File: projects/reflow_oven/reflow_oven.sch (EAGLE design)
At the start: 5 parts, among them IC1 MEGA32-A, IC3 FT232RL, X1 MINI-USB_SHIELD5P4-32005-400

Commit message: think the ftdi chip is done.  also did a good deal of the arduino setup.
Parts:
- added C2, C4, C9: 0.1uF, rcl:C-EUC0805
- added C3, C7, C8: 10uF, adafruit:CPOL-US175TMP-0810
- added C5, C6: 22pF, rcl:C-EUC0805
- added IC2: 7805DT, linear:7805DT
- added LED1: Red, led:LEDCHIPLED_0603
- added LED2: Green, led:LEDCHIPLED_0603
- added POWERLED: Green, adafruit:LEDCHIP-LED0805
- added R1, R2: 1k, resistor:R-US_R0805
- added R3: 10k, resistor:R-US_R0805
- added R4: 150, resistor:R-US_R0805
- added X2: 16.000MHz, adafruit:XTALNX8045
- C1: value (none) -> 0.1uF; device rcl:C-USC0805K -> rcl:C-EUC0805
- X1: value MINI-USB_SHIELD5P4-32005-400 -> USB; device con-cypressindustries:MINI-USB_SHIELD5P4-32005-400 -> con-cypressindustries:MINI-USB-32005-201
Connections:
- net RXD renamed 0
- net TXD renamed 1
- new net 10: IC1.(AIN0/INT2)PB2
- new net 11: IC1.(AIN1/OC0)PB3
- new net 12: IC1.(SS)PB4
- new net 13: IC1.(MOSI)PB5
- new net 8: IC1.(T0/XCK)PB0
- new net 9: IC1.(T1)PB1
- new net A1: IC1.(TDO)PC4
- new net A2: IC1.(TMS)PC3
- new net A3: IC1.(TCK)PC2
- new net A4: IC1.PC1(SDA)
- new net A5: IC1.PC0(SCL)
- new net D+DP: IC3.USBDP, X1.3
- new net D-DM: IC3.USBDM, X1.2
- new net DTR: C4.2, IC3.!DTR
- new net N$1: C5.2, IC1.XTAL2, X2.P$2
- new net N$10: IC1.(ICP)PD6
- new net N$11: IC1.(OC2)PD7
- new net N$17: IC1.(TDI)PC5
- new net N$18: IC1.(TOSC1)PC6
- new net N$19: IC1.(TOSC2)PC7
- new net N$2: C6.2, IC1.XTAL1, X2.P$1
- new net N$4: LED1.A, R1.1
- new net N$5: POWERLED.C, R4.2
- new net N$6: IC1.(INT0)PD2
- new net N$7: IC1.(INT1)PD3
- new net N$8: IC1.(OC1B)PD4
- new net N$9: IC1.(OC1A)PD5
- new net POWER: IC3.VCCIO
- new net RXLED: IC3.CBUS1, LED2.C
- new net TXLED: IC3.CBUS0, LED1.C
- new net VCCIO: C1.1, IC3.3V3OUT
- new net VIN: C7.+, IC2.VI
- new net VOUT: C8.+, IC2.VO, POWERLED.A
- net GND: now also C1.2, C2.2, C3.-, C5.1, C6.1, C7.-, C8.-, C9.1, IC2.GND, IC3.TEST, R4.1, X1.5
- net N$3: now also LED2.A, R2.1; no longer C1.1, IC3.!RESET
- net RESET: now also C4.1, R3.2; no longer C1.2
- net VCC: now also C2.1, C3.+, C9.2, IC1.AREF, IC3.VCC, R1.2, R2.2, R3.1, X1.1
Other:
- note added: "3.3V"
- note added: "Check These Names"

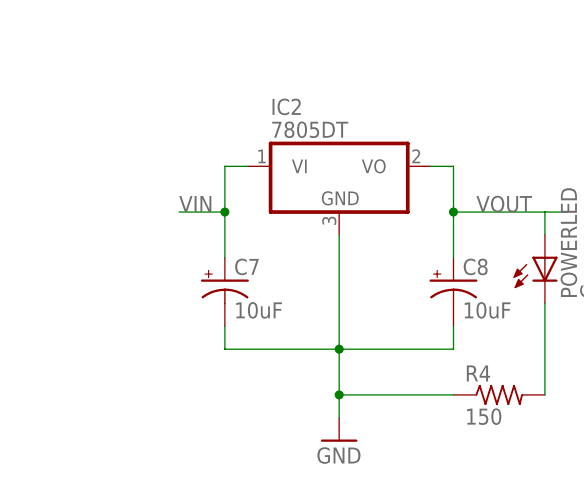
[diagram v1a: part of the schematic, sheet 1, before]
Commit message: add DC Jack
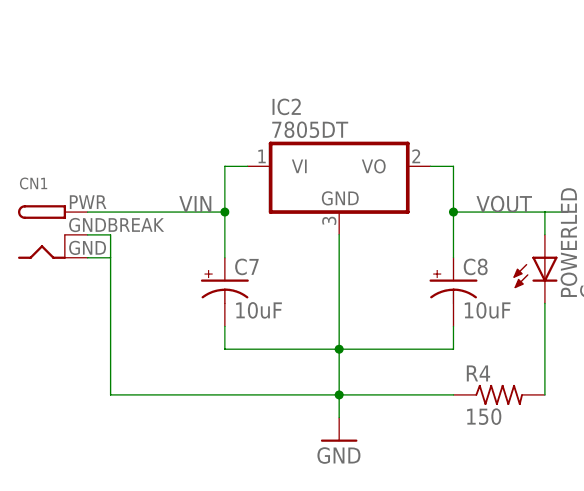
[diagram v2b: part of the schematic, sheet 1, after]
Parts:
- added CN1: (no value), adafruit:DCBARRELPTH
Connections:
- net GND: now also CN1.GND, CN1.GNDBREAK
- net VIN: now also CN1.PWR
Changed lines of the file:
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@@
 <grid distance="0.1" unitdist="inch" unit="inch" style="lines" multiple="1" display="no" altdistance="0.01" altunitdist="inch" altunit="inch"/>
 <layers>
-<layer number="1" name="Top" color="4" fill="1" visible="yes" active="no"/>
-<layer number="2" name="Route2" color="1" fill="3" visible="yes" active="no"/>
-<layer number="3" name="Route3" color="4" fill="3" visible="yes" active="no"/>
-<layer number="4" name="Route4" color="1" fill="4" visible="yes" active="no"/>
-<layer number="5" name="Route5" color="4" fill="4" visible="yes" active="no"/>
-<layer number="6" name="Route6" color="1" fill="8" visible="yes" active="no"/>
-<layer number="7" name="Route7" color="4" fill="8" visible="yes" active="no"/>
-<layer number="8" name="Route8" color="1" fill="2" visible="yes" active="no"/>
-<layer number="9" name="Route9" color="4" fill="2" visible="yes" active="no"/>
-<layer number="10" name="Route10" color="1" fill="7" visible="yes" active="no"/>
-<layer number="11" name="Route11" color="4" fill="7" visible="yes" active="no"/>
-<layer number="12" name="Route12" color="1" fill="5" visible="yes" active="no"/>
-<layer number="13" name="Route13" color="4" fill="5" visible="yes" active="no"/>
-<layer number="14" name="Route14" color="1" fill="6" visible="yes" active="no"/>
-<layer number="15" name="Route15" color="4" fill="6" visible="yes" active="no"/>
-<layer number="16" name="Bottom" color="1" fill="1" visible="yes" active="no"/>
-<layer number="17" name="Pads" color="2" fill="1" visible="yes" active="no"/>
-<layer number="18" name="Vias" color="2" fill="1" visible="yes" active="no"/>
-<layer number="19" name="Unrouted" color="6" fill="1" visible="yes" active="no"/>
-<layer number="20" name="Dimension" color="15" fill="1" visible="yes" active="no"/>
-<layer number="21" name="tPlace" color="7" fill="1" visible="yes" active="no"/>
-<layer number="22" name="bPlace" color="7" fill="1" visible="yes" active="no"/>
-<layer number="23" name="tOrigins" color="15" fill="1" visible="yes" active="no"/>
-<layer number="24" name="bOrigins" color="15" fill="1" visible="yes" active="no"/>
-<layer number="25" name="tNames" color="7" fill="1" visible="yes" active="no"/>
-<layer number="26" name="bNames" color="7" fill="1" visible="yes" active="no"/>
-<layer number="27" name="tValues" color="7" fill="1" visible="yes" active="no"/>
-<layer number="28" name="bValues" color="7" fill="1" visible="yes" active="no"/>
+<layer number="1" name="Top" color="4" fill="1" visible="no" active="no"/>
+<layer number="2" name="Route2" color="1" fill="3" visible="no" active="no"/>
+<layer number="3" name="Route3" color="4" fill="3" visible="no" active="no"/>
+<layer number="4" name="Route4" color="1" fill="4" visible="no" active="no"/>
+<layer number="5" name="Route5" color="4" fill="4" visible="no" active="no"/>
+<layer number="6" name="Route6" color="1" fill="8" visible="no" active="no"/>
+<layer number="7" name="Route7" color="4" fill="8" visible="no" active="no"/>
+<layer number="8" name="Route8" color="1" fill="2" visible="no" active="no"/>
+<layer number="9" name="Route9" color="4" fill="2" visible="no" active="no"/>
+<layer number="10" name="Route10" color="1" fill="7" visible="no" active="no"/>
+<layer number="11" name="Route11" color="4" fill="7" visible="no" active="no"/>
+<layer number="12" name="Route12" color="1" fill="5" visible="no" active="no"/>
+<layer number="13" name="Route13" color="4" fill="5" visible="no" active="no"/>
+<layer number="14" name="Route14" color="1" fill="6" visible="no" active="no"/>
+<layer number="15" name="Route15" color="4" fill="6" visible="no" active="no"/>
+<layer number="16" name="Bottom" color="1" fill="1" visible="no" active="no"/>
+<layer number="17" name="Pads" color="2" fill="1" visible="no" active="no"/>
+<layer number="18" name="Vias" color="2" fill="1" visible="no" active="no"/>
+<layer number="19" name="Unrouted" color="6" fill="1" visible="no" active="no"/>
+<layer number="20" name="Dimension" color="15" fill="1" visible="no" active="no"/>
+<layer number="21" name="tPlace" color="7" fill="1" visible="no" active="no"/>
+<layer number="22" name="bPlace" color="7" fill="1" visible="no" active="no"/>
+<layer number="23" name="tOrigins" color="15" fill="1" visible="no" active="no"/>
+<layer number="24" name="bOrigins" color="15" fill="1" visible="no" active="no"/>
+<layer number="25" name="tNames" color="7" fill="1" visible="no" active="no"/>
+<layer number="26" name="bNames" color="7" fill="1" visible="no" active="no"/>
+<layer number="27" name="tValues" color="7" fill="1" visible="no" active="no"/>
+<layer number="28" name="bValues" color="7" fill="1" visible="no" active="no"/>
 <layer number="29" name="tStop" color="7" fill="3" visible="no" active="no"/>
 <layer number="30" name="bStop" color="7" fill="6" visible="no" active="no"/>
@@
 <layer number="35" name="tGlue" color="7" fill="4" visible="no" active="no"/>
 <layer number="36" name="bGlue" color="7" fill="5" visible="no" active="no"/>
-<layer number="37" name="tTest" color="7" fill="1" visible="yes" active="no"/>
-<layer number="38" name="bTest" color="7" fill="1" visible="yes" active="no"/>
+<layer number="37" name="tTest" color="7" fill="1" visible="no" active="no"/>
+<layer number="38" name="bTest" color="7" fill="1" visible="no" active="no"/>
 <layer number="39" name="tKeepout" color="4" fill="11" visible="no" active="no"/>
 <layer number="40" name="bKeepout" color="1" fill="11" visible="no" active="no"/>
@@
 <layer number="44" name="Drills" color="7" fill="1" visible="no" active="no"/>
 <layer number="45" name="Holes" color="7" fill="1" visible="no" active="no"/>
-<layer number="46" name="Milling" color="3" fill="1" visible="yes" active="no"/>
-<layer number="47" name="Measures" color="7" fill="1" visible="yes" active="no"/>
-<layer number="48" name="Document" color="7" fill="1" visible="yes" active="no"/>
-<layer number="49" name="Reference" color="7" fill="1" visible="yes" active="no"/>
-<layer number="50" name="dxf" color="7" fill="1" visible="yes" active="no"/>
-<layer number="51" name="tDocu" color="7" fill="1" visible="yes" active="no"/>
-<layer number="52" name="bDocu" color="7" fill="1" visible="yes" active="no"/>
-<layer number="53" name="tGND_GNDA" color="7" fill="9" visible="yes" active="no"/>
-<layer number="54" name="bGND_GNDA" color="1" fill="9" visible="yes" active="no"/>
-<layer number="56" name="wert" color="7" fill="1" visible="yes" active="no"/>
+<layer number="46" name="Milling" color="3" fill="1" visible="no" active="no"/>
+<layer number="47" name="Measures" color="7" fill="1" visible="no" active="no"/>
+<layer number="48" name="Document" color="7" fill="1" visible="no" active="no"/>
+<layer number="49" name="Reference" color="7" fill="1" visible="no" active="no"/>
+<layer number="50" name="dxf" color="7" fill="1" visible="no" active="no"/>
+<layer number="51" name="tDocu" color="7" fill="1" visible="no" active="no"/>
+<layer number="52" name="bDocu" color="7" fill="1" visible="no" active="no"/>
+<layer number="53" name="tGND_GNDA" color="7" fill="9" visible="no" active="no"/>
+<layer number="54" name="bGND_GNDA" color="1" fill="9" visible="no" active="no"/>
+<layer number="56" name="wert" color="7" fill="1" visible="no" active="no"/>
 <layer number="91" name="Nets" color="2" fill="1" visible="yes" active="yes"/>
 <layer number="92" name="Busses" color="1" fill="1" visible="yes" active="yes"/>
@@
 <part name="C9" library="rcl" deviceset="C-EU" device="C0805" value="0.1uF"/>
 <part name="GND4" library="supply1" deviceset="GND" device=""/>
+<part name="CN1" library="adafruit" deviceset="DCBARREL" device="PTH"/>
 </parts>
 <sheets>
@@
 </instance>
 <instance part="GND4" gate="1" x="88.9" y="111.76"/>
+<instance part="CN1" gate="G$1" x="20.32" y="76.2"/>
 </instances>
 <busses>
@@
 <wire x1="63.5" y1="58.42" x2="50.8" y2="58.42" width="0.1524" layer="91"/>
 <junction x="50.8" y="58.42"/>
+<pinref part="CN1" gate="G$1" pin="GNDBREAK"/>
+<wire x1="22.86" y1="76.2" x2="25.4" y2="76.2" width="0.1524" layer="91"/>
+<wire x1="25.4" y1="76.2" x2="25.4" y2="73.66" width="0.1524" layer="91"/>
+<pinref part="CN1" gate="G$1" pin="GND"/>
+<wire x1="25.4" y1="73.66" x2="22.86" y2="73.66" width="0.1524" layer="91"/>
+<wire x1="25.4" y1="73.66" x2="25.4" y2="58.42" width="0.1524" layer="91"/>
+<wire x1="25.4" y1="58.42" x2="50.8" y2="58.42" width="0.1524" layer="91"/>
 </segment>
 <segment>
@@
 <junction x="38.1" y="78.74"/>
 <wire x1="38.1" y1="78.74" x2="38.1" y2="73.66" width="0.1524" layer="91"/>
-<wire x1="38.1" y1="78.74" x2="33.02" y2="78.74" width="0.1524" layer="91"/>
 <label x="33.02" y="78.74" size="1.778" layer="95"/>
-</segment>
-</net>
+<pinref part="CN1" gate="G$1" pin="PWR"/>
+<wire x1="22.86" y1="78.74" x2="38.1" y2="78.74" width="0.1524" layer="91"/>
+</segment>
+</net>

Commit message: button debounce start
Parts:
- added C10, C11: 1uF, resistor:C-USC0805
- added C12: 100nF, resistor:C-USC0805
- added D1, D2: (no value), adafruit:DIODESMA
- added IC4: 74HC14D, 74xx-eu:74HC14D
- added R5, R6: 82k, resistor:R-US_R0805
- added R7, R8: 18k, resistor:R-US_R0805
- added S2, S3: (no value), switch-omron:10-XX
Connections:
- new net 2: IC4B.O
- new net 3: IC4A.O
- new net N$12: D1.A, R5.2, R8.1, S2.S, S2.S1
- new net N$13: C11.1, D1.C, IC4A.I, R8.2
- new net N$14: D2.A, R6.2, R7.1, S3.S, S3.S1
- new net N$15: C10.1, D2.C, IC4B.I, R7.2
- net GND: now also C10.2, C11.2, C12.2, IC4P.GND, S2.P, S2.P1, S3.P, S3.P1
- net VCC: now also C12.1, IC4P.VCC, R5.1, R6.1
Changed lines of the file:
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@@
 <part name="GND4" library="supply1" deviceset="GND" device=""/>
 <part name="CN1" library="adafruit" deviceset="DCBARREL" device="PTH"/>
+<part name="IC4" library="74xx-eu" deviceset="74*14" device="D" technology="HC"/>
+<part name="P+5" library="supply1" deviceset="VCC" device=""/>
+<part name="P+9" library="supply1" deviceset="VCC" device=""/>
+<part name="R5" library="resistor" deviceset="R-US_" device="R0805" value="82k"/>
+<part name="R8" library="resistor" deviceset="R-US_" device="R0805" value="18k"/>
+<part name="GND13" library="supply1" deviceset="GND" device=""/>
+<part name="GND14" library="supply1" deviceset="GND" device=""/>
+<part name="D1" library="adafruit" deviceset="DIODE" device="SMA"/>
+<part name="C11" library="resistor" deviceset="C-US" device="C0805" value="1uF"/>
+<part name="C12" library="resistor" deviceset="C-US" device="C0805" value="100nF"/>
+<part name="S2" library="switch-omron" deviceset="10-XX" device=""/>
+<part name="P+10" library="supply1" deviceset="VCC" device=""/>
+<part name="R6" library="resistor" deviceset="R-US_" device="R0805" value="82k"/>
+<part name="R7" library="resistor" deviceset="R-US_" device="R0805" value="18k"/>
+<part name="GND15" library="supply1" deviceset="GND" device=""/>
+<part name="D2" library="adafruit" deviceset="DIODE" device="SMA"/>
+<part name="C10" library="resistor" deviceset="C-US" device="C0805" value="1uF"/>
+<part name="S3" library="switch-omron" deviceset="10-XX" device=""/>
+<part name="FRAME4" library="frames" deviceset="DINA4_L" device=""/>
+<part name="FRAME5" library="frames" deviceset="LETTER_P" device=""/>
 </parts>
 <sheets>
@@
 </nets>
 </sheet>
+<sheet>
+<description>button debounce</description>
+<plain>
+</plain>
+<instances>
+<instance part="IC4" gate="A" x="99.06" y="132.08"/>
+<instance part="IC4" gate="B" x="99.06" y="96.52"/>
+<instance part="P+5" gate="VCC" x="25.4" y="157.48"/>
+<instance part="P+9" gate="VCC" x="147.32" y="149.86"/>
+<instance part="R5" gate="G$1" x="35.56" y="147.32"/>
+<instance part="R8" gate="G$1" x="50.8" y="137.16"/>
+<instance part="GND13" gate="1" x="147.32" y="119.38"/>
+<instance part="GND14" gate="1" x="50.8" y="116.84"/>
+<instance part="D1" gate="G$1" x="50.8" y="147.32"/>
+<instance part="C11" gate="G$1" x="58.42" y="132.08"/>
+<instance part="C12" gate="G$1" x="152.4" y="137.16"/>
+<instance part="S2" gate="1" x="40.64" y="127"/>
+<instance part="P+10" gate="VCC" x="25.4" y="111.76"/>
+<instance part="R6" gate="G$1" x="35.56" y="101.6"/>
+<instance part="R7" gate="G$1" x="50.8" y="91.44"/>
+<instance part="GND15" gate="1" x="50.8" y="71.12"/>
+<instance part="D2" gate="G$1" x="50.8" y="101.6"/>
+<instance part="C10" gate="G$1" x="58.42" y="86.36"/>
+<instance part="S3" gate="1" x="40.64" y="81.28"/>
+<instance part="IC4" gate="P" x="142.24" y="134.62"/>
+<instance part="FRAME5" gate="G$1" x="0" y="0"/>
+<instance part="FRAME5" gate="G$2" x="83.82" y="0"/>
+</instances>
+<busses>
+</busses>
+<nets>
+<net name="VCC" class="0">
+<segment>
+<pinref part="P+5" gate="VCC" pin="VCC"/>
+<wire x1="25.4" y1="154.94" x2="25.4" y2="147.32" width="0.1524" layer="91"/>
+<pinref part="R5" gate="G$1" pin="1"/>
+<wire x1="25.4" y1="147.32" x2="30.48" y2="147.32" width="0.1524" layer="91"/>
+</segment>
+<segment>
+<pinref part="P+10" gate="VCC" pin="VCC"/>
+<wire x1="25.4" y1="109.22" x2="25.4" y2="101.6" width="0.1524" layer="91"/>
+<pinref part="R6" gate="G$1" pin="1"/>
+<wire x1="25.4" y1="101.6" x2="30.48" y2="101.6" width="0.1524" layer="91"/>
+</segment>
+<segment>
+<pinref part="IC4" gate="P" pin="VCC"/>
+<wire x1="142.24" y1="142.24" x2="142.24" y2="144.78" width="0.1524" layer="91"/>
+<wire x1="142.24" y1="144.78" x2="147.32" y2="144.78" width="0.1524" layer="91"/>
+<pinref part="C12" gate="G$1" pin="1"/>
+<wire x1="147.32" y1="144.78" x2="152.4" y2="144.78" width="0.1524" layer="91"/>
+<wire x1="152.4" y1="144.78" x2="152.4" y2="139.7" width="0.1524" layer="91"/>
+<pinref part="P+9" gate="VCC" pin="VCC"/>
+<wire x1="147.32" y1="147.32" x2="147.32" y2="144.78" width="0.1524" layer="91"/>
+<junction x="147.32" y="144.78"/>
+</segment>
+</net>
+<net name="N$12" class="0">
+<segment>
+<pinref part="R5" gate="G$1" pin="2"/>
+<pinref part="D1" gate="G$1" pin="A"/>
+<wire x1="40.64" y1="147.32" x2="43.18" y2="147.32" width="0.1524" layer="91"/>
+<pinref part="R8" gate="G$1" pin="1"/>
+<wire x1="43.18" y1="147.32" x2="48.26" y2="147.32" width="0.1524" layer="91"/>
+<wire x1="45.72" y1="137.16" x2="43.18" y2="137.16" width="0.1524" layer="91"/>
+<wire x1="43.18" y1="137.16" x2="43.18" y2="147.32" width="0.1524" layer="91"/>
+<junction x="43.18" y="147.32"/>
+<junction x="43.18" y="137.16"/>
+<wire x1="43.18" y1="137.16" x2="43.18" y2="132.08" width="0.1524" layer="91"/>
+<pinref part="S2" gate="1" pin="S1"/>
+<pinref part="S2" gate="1" pin="S"/>
+<wire x1="40.64" y1="132.08" x2="43.18" y2="132.08" width="0.1524" layer="91"/>
+<junction x="43.18" y="132.08"/>
+</segment>
+</net>
+<net name="N$13" class="0">
+<segment>
+<pinref part="D1" gate="G$1" pin="C"/>
+<wire x1="53.34" y1="147.32" x2="58.42" y2="147.32" width="0.1524" layer="91"/>
+<wire x1="58.42" y1="147.32" x2="58.42" y2="137.16" width="0.1524" layer="91"/>
+<pinref part="R8" gate="G$1" pin="2"/>
+<wire x1="55.88" y1="137.16" x2="58.42" y2="137.16" width="0.1524" layer="91"/>
+<pinref part="C11" gate="G$1" pin="1"/>
+<wire x1="58.42" y1="137.16" x2="58.42" y2="134.62" width="0.1524" layer="91"/>
+<junction x="58.42" y="137.16"/>
+<wire x1="58.42" y1="137.16" x2="71.12" y2="137.16" width="0.1524" layer="91"/>
+<wire x1="71.12" y1="137.16" x2="71.12" y2="132.08" width="0.1524" layer="91"/>
+<pinref part="IC4" gate="A" pin="I"/>
+<wire x1="71.12" y1="132.08" x2="88.9" y2="132.08" width="0.1524" layer="91"/>
+</segment>
+</net>
+<net name="GND" class="0">
+<segment>
+<pinref part="C11" gate="G$1" pin="2"/>
+<wire x1="58.42" y1="127" x2="58.42" y2="119.38" width="0.1524" layer="91"/>
+<pinref part="GND14" gate="1" pin="GND"/>
+<wire x1="50.8" y1="119.38" x2="58.42" y2="119.38" width="0.1524" layer="91"/>
+<wire x1="50.8" y1="119.38" x2="43.18" y2="119.38" width="0.1524" layer="91"/>
+<wire x1="43.18" y1="119.38" x2="43.18" y2="121.92" width="0.1524" layer="91"/>
+<pinref part="S2" gate="1" pin="P1"/>
+<pinref part="S2" gate="1" pin="P"/>
+<wire x1="40.64" y1="121.92" x2="43.18" y2="121.92" width="0.1524" layer="91"/>
+<junction x="43.18" y="121.92"/>
+</segment>
+<segment>
+<pinref part="C10" gate="G$1" pin="2"/>
+<wire x1="58.42" y1="81.28" x2="58.42" y2="73.66" width="0.1524" layer="91"/>
+<pinref part="GND15" gate="1" pin="GND"/>
+<wire x1="50.8" y1="73.66" x2="58.42" y2="73.66" width="0.1524" layer="91"/>
+<wire x1="50.8" y1="73.66" x2="43.18" y2="73.66" width="0.1524" layer="91"/>
+<wire x1="43.18" y1="73.66" x2="43.18" y2="76.2" width="0.1524" layer="91"/>
+<pinref part="S3" gate="1" pin="P1"/>
+<pinref part="S3" gate="1" pin="P"/>
+<wire x1="40.64" y1="76.2" x2="43.18" y2="76.2" width="0.1524" layer="91"/>
+<junction x="43.18" y="76.2"/>
+</segment>
+<segment>
+<pinref part="IC4" gate="P" pin="GND"/>
+<wire x1="142.24" y1="127" x2="142.24" y2="124.46" width="0.1524" layer="91"/>
+<wire x1="142.24" y1="124.46" x2="147.32" y2="124.46" width="0.1524" layer="91"/>
+<pinref part="C12" gate="G$1" pin="2"/>
+<wire x1="147.32" y1="124.46" x2="152.4" y2="124.46" width="0.1524" layer="91"/>
+<wire x1="152.4" y1="124.46" x2="152.4" y2="132.08" width="0.1524" layer="91"/>
+<pinref part="GND13" gate="1" pin="GND"/>
+<wire x1="147.32" y1="124.46" x2="147.32" y2="121.92" width="0.1524" layer="91"/>
+<junction x="147.32" y="124.46"/>
+</segment>
+</net>
+<net name="N$14" class="0">
+<segment>
+<pinref part="R6" gate="G$1" pin="2"/>
+<pinref part="D2" gate="G$1" pin="A"/>
+<wire x1="40.64" y1="101.6" x2="43.18" y2="101.6" width="0.1524" layer="91"/>
+<pinref part="R7" gate="G$1" pin="1"/>
+<wire x1="43.18" y1="101.6" x2="48.26" y2="101.6" width="0.1524" layer="91"/>
+<wire x1="45.72" y1="91.44" x2="43.18" y2="91.44" width="0.1524" layer="91"/>
+<wire x1="43.18" y1="91.44" x2="43.18" y2="101.6" width="0.1524" layer="91"/>
+<junction x="43.18" y="101.6"/>
+<junction x="43.18" y="91.44"/>
+<wire x1="43.18" y1="91.44" x2="43.18" y2="86.36" width="0.1524" layer="91"/>
+<pinref part="S3" gate="1" pin="S1"/>
+<pinref part="S3" gate="1" pin="S"/>
+<wire x1="40.64" y1="86.36" x2="43.18" y2="86.36" width="0.1524" layer="91"/>
+<junction x="43.18" y="86.36"/>
+</segment>
+</net>
+<net name="N$15" class="0">
+<segment>
+<pinref part="D2" gate="G$1" pin="C"/>
+<wire x1="53.34" y1="101.6" x2="58.42" y2="101.6" width="0.1524" layer="91"/>
+<wire x1="58.42" y1="101.6" x2="58.42" y2="91.44" width="0.1524" layer="91"/>
+<pinref part="R7" gate="G$1" pin="2"/>
+<wire x1="55.88" y1="91.44" x2="58.42" y2="91.44" width="0.1524" layer="91"/>
+<pinref part="C10" gate="G$1" pin="1"/>
+<wire x1="58.42" y1="91.44" x2="58.42" y2="88.9" width="0.1524" layer="91"/>
+<junction x="58.42" y="91.44"/>
+<wire x1="58.42" y1="91.44" x2="71.12" y2="91.44" width="0.1524" layer="91"/>
+<wire x1="71.12" y1="91.44" x2="71.12" y2="96.52" width="0.1524" layer="91"/>
+<pinref part="IC4" gate="B" pin="I"/>
+<wire x1="71.12" y1="96.52" x2="88.9" y2="96.52" width="0.1524" layer="91"/>
+</segment>
+</net>
+<net name="2" class="0">
+<segment>
+<pinref part="IC4" gate="B" pin="O"/>
+<wire x1="109.22" y1="96.52" x2="114.3" y2="96.52" width="0.1524" layer="91"/>
+<label x="116.84" y="96.52" size="1.778" layer="95"/>
+</segment>
+</net>
+<net name="3" class="0">
+<segment>
+<pinref part="IC4" gate="A" pin="O"/>
+<wire x1="109.22" y1="132.08" x2="114.3" y2="132.08" width="0.1524" layer="91"/>
+<label x="116.84" y="132.08" size="1.778" layer="95"/>
+</segment>
+</net>
+</nets>
+</sheet>
+<sheet>
+<plain>
+</plain>
+<instances>
+<instance part="FRAME4" gate="G$1" x="0" y="0"/>
+<instance part="FRAME4" gate="G$2" x="162.56" y="0"/>
+</instances>
+<busses>
+</busses>
+<nets>
+</nets>
+</sheet>
